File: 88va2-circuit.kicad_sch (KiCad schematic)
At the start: 0 parts

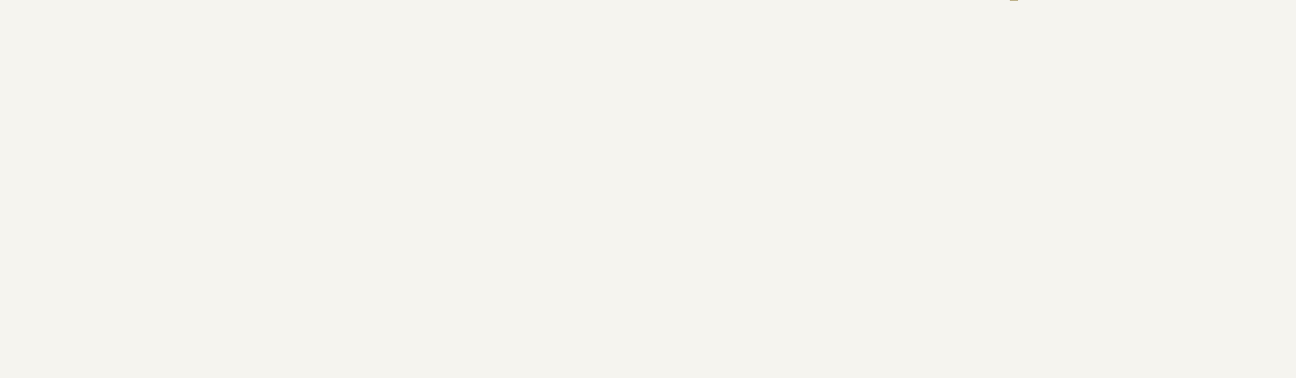
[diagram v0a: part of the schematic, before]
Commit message: schematic: add description
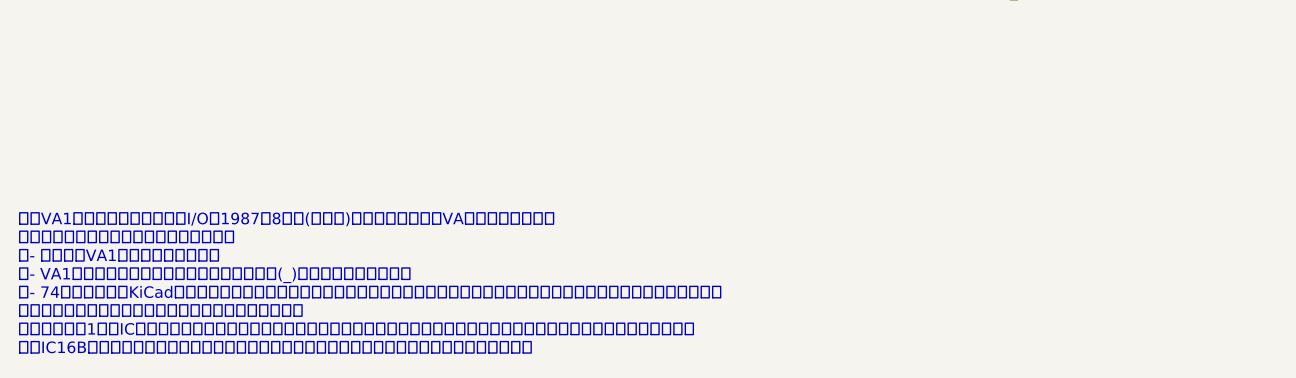
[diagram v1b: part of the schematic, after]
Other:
- note added: "・「VA1回路図」とは、雑誌「I/O」1987年8月号(工学社)に掲載された初代VAの回路図を指す。 ・ピン、信号の名称は次のとおりとした。 - 基本的にVA1回路図にならった。 - VA1回路図に該当のない信号はアンダーバー(_)で始まる名前とした。 - 74シリーズなどKiCadのライブラリで提供されているシンボルでは、そこで定義された名称をそのまま利用している場合がある。 ・配線は、実基板で結線が確認されたもののみを記載。 ・実基板上で1つのICであっても、この回路図では複数のシンボルで分割されて記載している場合がある。この場合、部品の番号は 「IC16B」のように実基板に記載の番号の末尾に英字の接尾辞が追加されたものとなっている。"
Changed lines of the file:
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@@
     (stroke (width 0) (type default))
+  )
+  (text "・「VA1回路図」とは、雑誌「I/O」1987年8月号(工学社)に掲載された初代VAの回路図を指す。\n・ピン、信号の名称は次のとおりとした。\n　- 基本的にVA1回路図にならった。\n　- VA1回路図に該当のない信号はアンダーバー(_)で始まる名前とした。\n　- 74シリーズなどKiCadのライブラリで提供されているシンボルでは、そこで定義された名称をそのまま利用している場合がある。\n・配線は、実基板で結線が確認されたもののみを記載。\n・実基板上で1つのICであっても、この回路図では複数のシンボルで分割されて記載している場合がある。この場合、部品の番号は\n　「IC16B」のように実基板に記載の番号の末尾に英字の接尾辞が追加されたものとなっている。\n"
+    (at 19.05 181.61 0)
+    (effects (font (size 1.27 1.27)) (justify left bottom))
   )
   (global_label "BACKUP" (shape output) (at 45.72 59.69 0) (fields_autoplaced)
